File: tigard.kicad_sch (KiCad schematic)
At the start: 91 parts, among them J1 USB_C_Receptacle_USB2.0, J2 JTAG, J3 UART, J4 SPI, J5 CORTEX, J6 LA, J7 I2C, Q1 BSH103, SW1 TARGET, SW2 MODE, U1 AP7365-18, U2 AP7365-33, U3 FT2232HQ, U4 93LC46BT-I/OT, U5 SN74LVC8T245, U6 SN74LVC8T245, Y1 12MHz

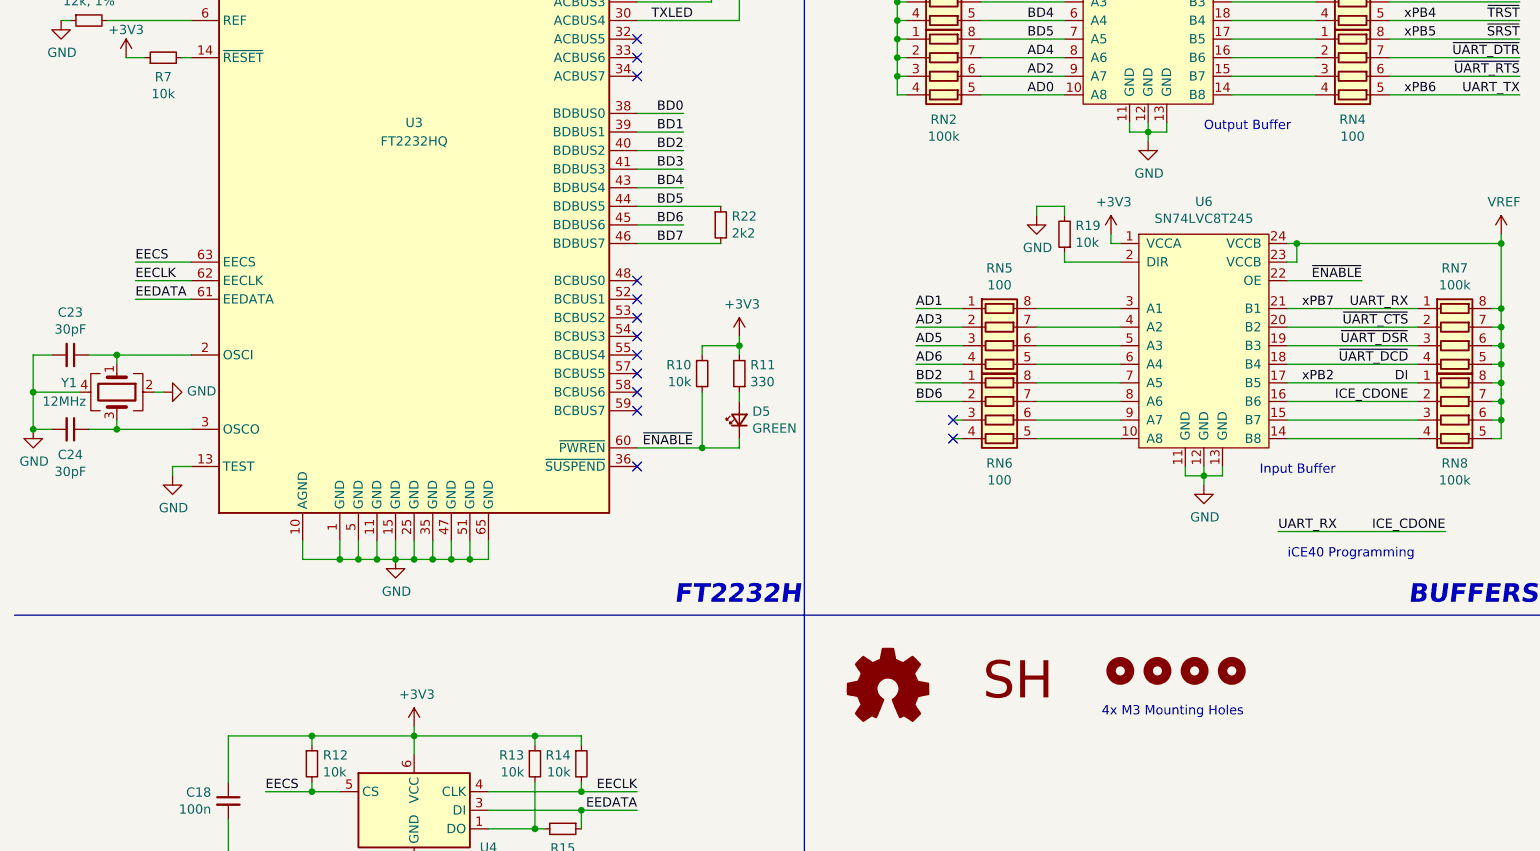
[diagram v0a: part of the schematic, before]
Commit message: tigard-lts: first pass at placement
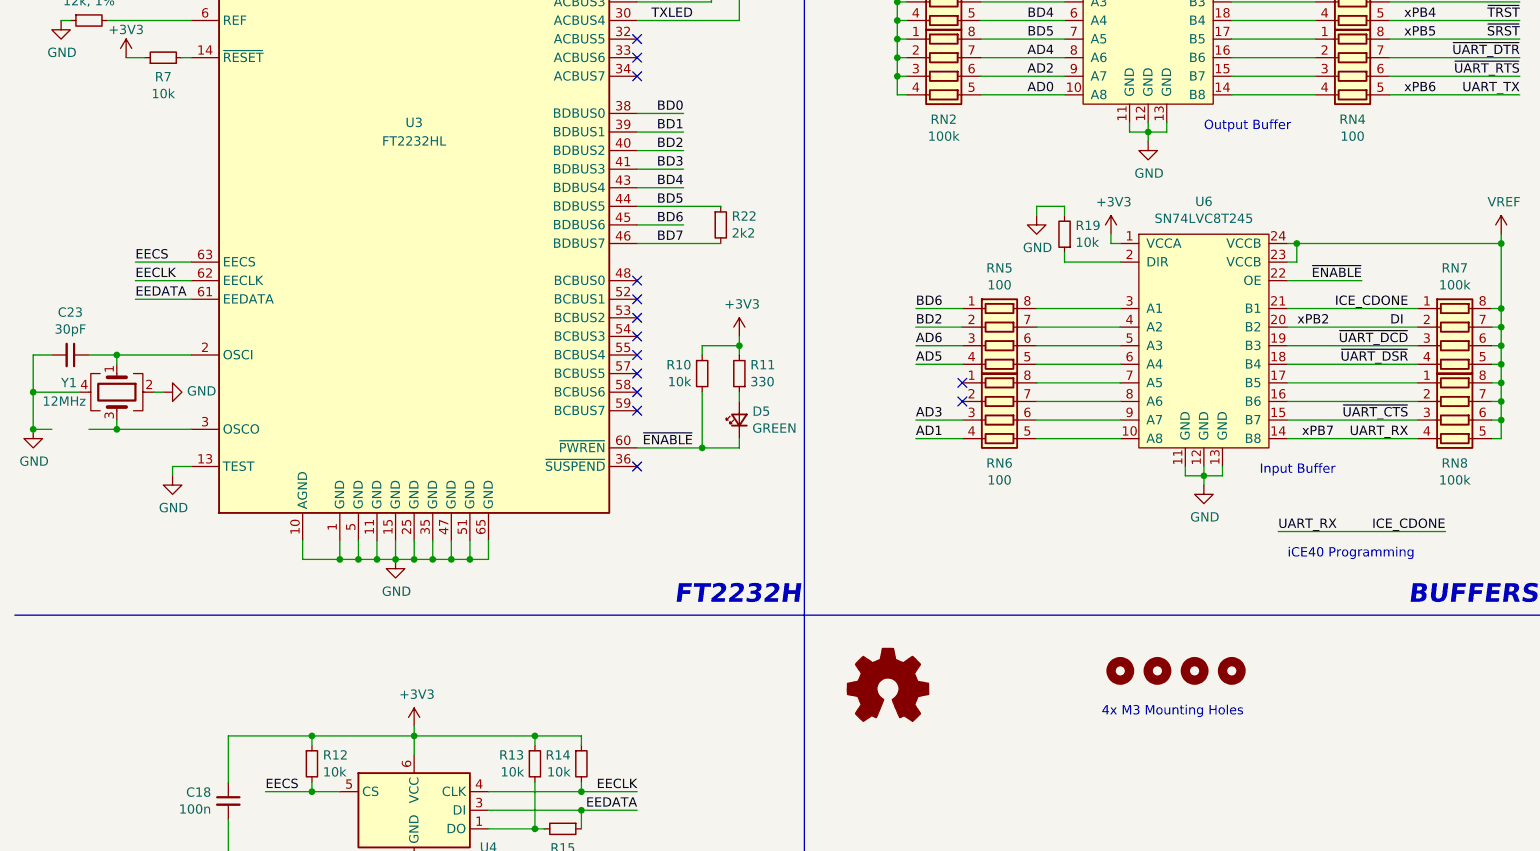
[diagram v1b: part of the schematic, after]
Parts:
- removed C24: 30pF, Capacitor_SMD:C_0402_1005Metric, symbol Device:C_Small
- removed LOGO2: Logo_SH, tigard:Securing_Hardware_Logo, symbol tigard:Logo_SH
- C1, C10, C11, C12, C13, C14, C15, C16, C17, C18, C19, C2, C20, C21, C22, C23, C25, C26, C3, C4, C5, C6, C7, C8, C9: footprint Capacitor_SMD:C_0402_1005Metric -> Capacitor_SMD:C_0805_2012Metric
- D1, D2, D3, D4, D5: footprint LED_SMD:LED_0603_1608Metric -> LED_SMD:LED_0805_2012Metric
- FB1, FB2, FB3: footprint Inductor_SMD:L_0402_1005Metric -> Inductor_SMD:L_0805_2012Metric
- R1, R10, R11, R12, R13, R14, R15, R16, R17, R18, R19, R2, R20, R21, R22, R24, R3, R4, R5, R6, R7, R8, R9: footprint Resistor_SMD:R_0402_1005Metric -> Inductor_SMD:L_0805_2012Metric
- RN1, RN2, RN3, RN4, RN5, RN6, RN7, RN8: footprint tigard:R_Array_Convex_4x0402_RoundRect -> Resistor_SMD:R_Array_Convex_4x0603
- U3: value FT2232HQ -> FT2232HL; footprint Package_DFN_QFN:QFN-64-1EP_9x9mm_P0.5mm_EP4.35x4.35mm_ThermalVias -> Package_QFP:LQFP-64_10x10mm_P0.5mm
- U5, U6: footprint Package_SO:TSSOP-24_4.4x7.8mm_P0.65mm -> Package_SO:SOIC-24W_7.5x15.4mm_P1.27mm
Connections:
- net AD1: now also RN6.4 (R4.1); no longer RN5.1 (R1.1)
- net AD3: now also RN6.3 (R3.1); no longer RN5.2 (R2.1)
- net AD5: now also RN5.4 (R4.1); no longer RN5.3 (R3.1)
- net AD6: now also RN5.3 (R3.1); no longer RN5.4 (R4.1)
- net BD2: now also RN5.2 (R2.1); no longer RN6.1 (R1.1)
- net BD6: now also RN5.1 (R1.1); no longer RN6.2 (R2.1)
- net DI: now also RN7.2 (R2.1), U6.20 (B2); no longer RN8.1 (R1.1), U6.17 (B5)
- net ICE_CDONE: now also RN8.4 (R4.1), U6.14 (B8); no longer RN8.2 (R2.1), U6.16 (B6)
- net ~{UART_CTS}: now also RN8.3 (R3.1), U6.15 (B7); no longer RN7.2 (R2.1), U6.20 (B2)
- net ~{UART_DCD}: now also RN7.3 (R3.1), U6.19 (B3); no longer RN7.4 (R4.1), U6.18 (B4)
- net ~{UART_DSR}: now also RN7.4 (R4.1), U6.18 (B4); no longer RN7.3 (R3.1), U6.19 (B3)
- new net: RN8.2 (R2.1), U6.16 (B6)
- new net: RN8.1 (R1.1), U6.17 (B5)

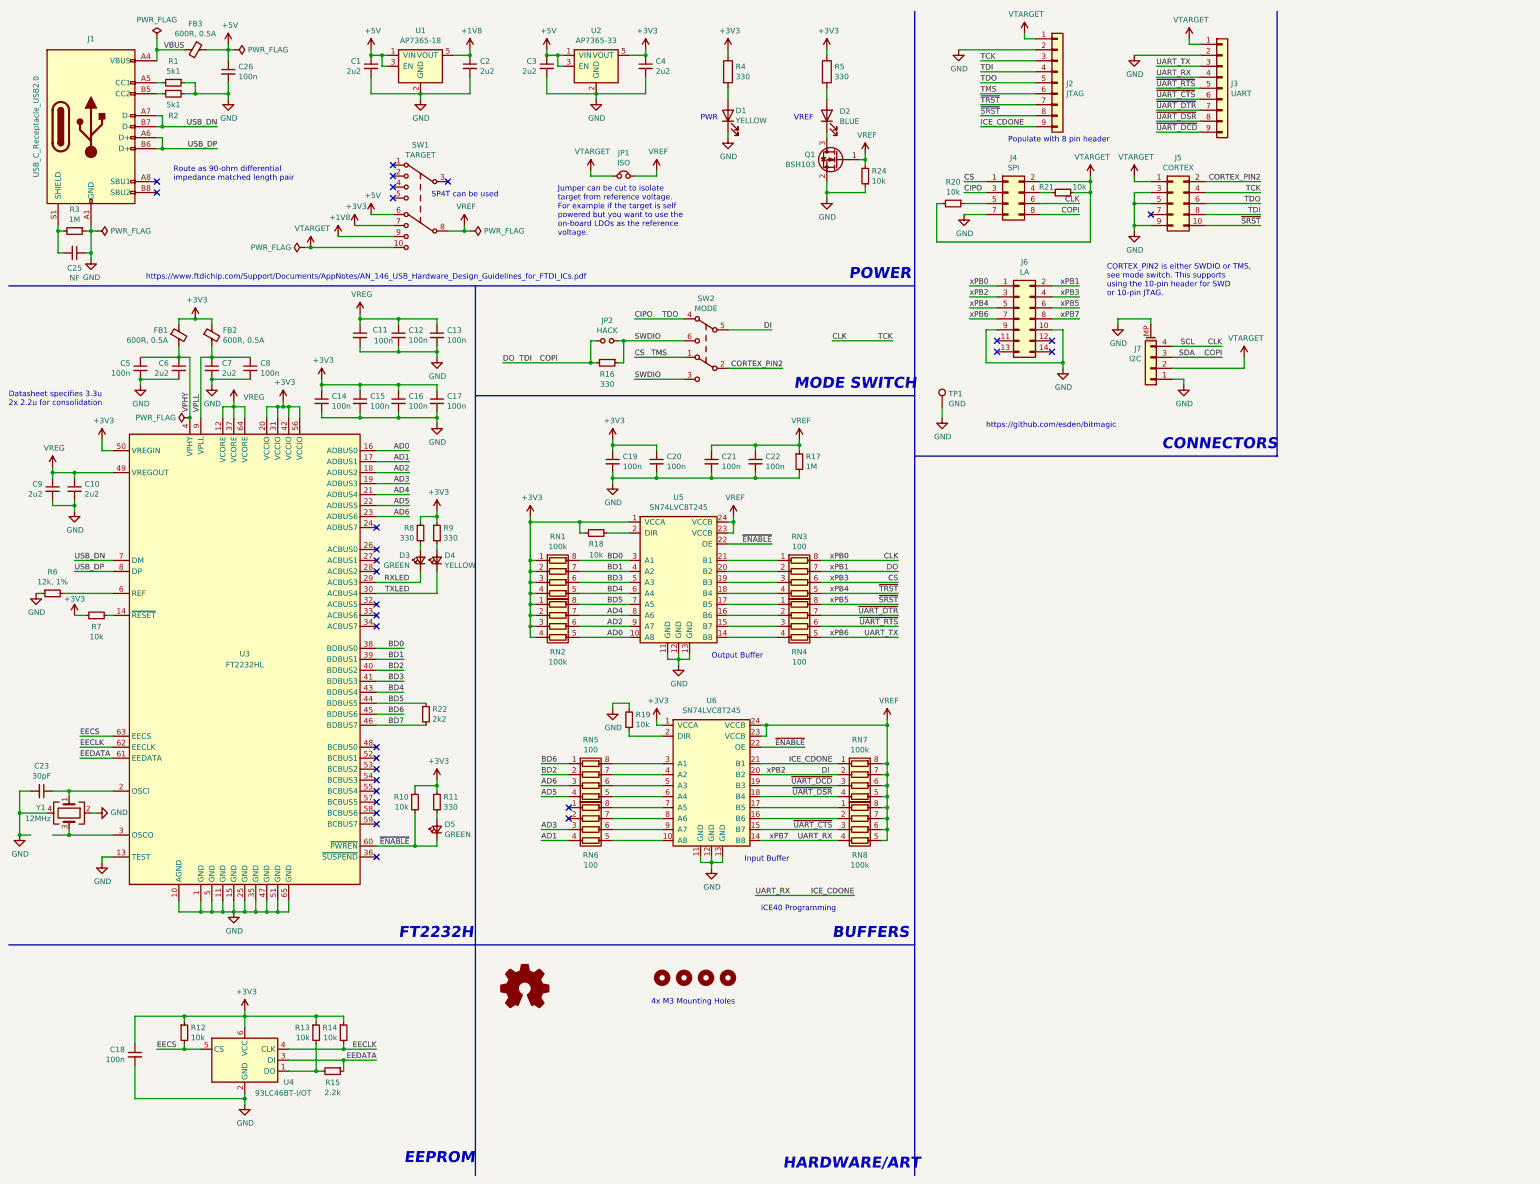
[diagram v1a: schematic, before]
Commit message: tomk-tigard-lts: progress commit - board outline
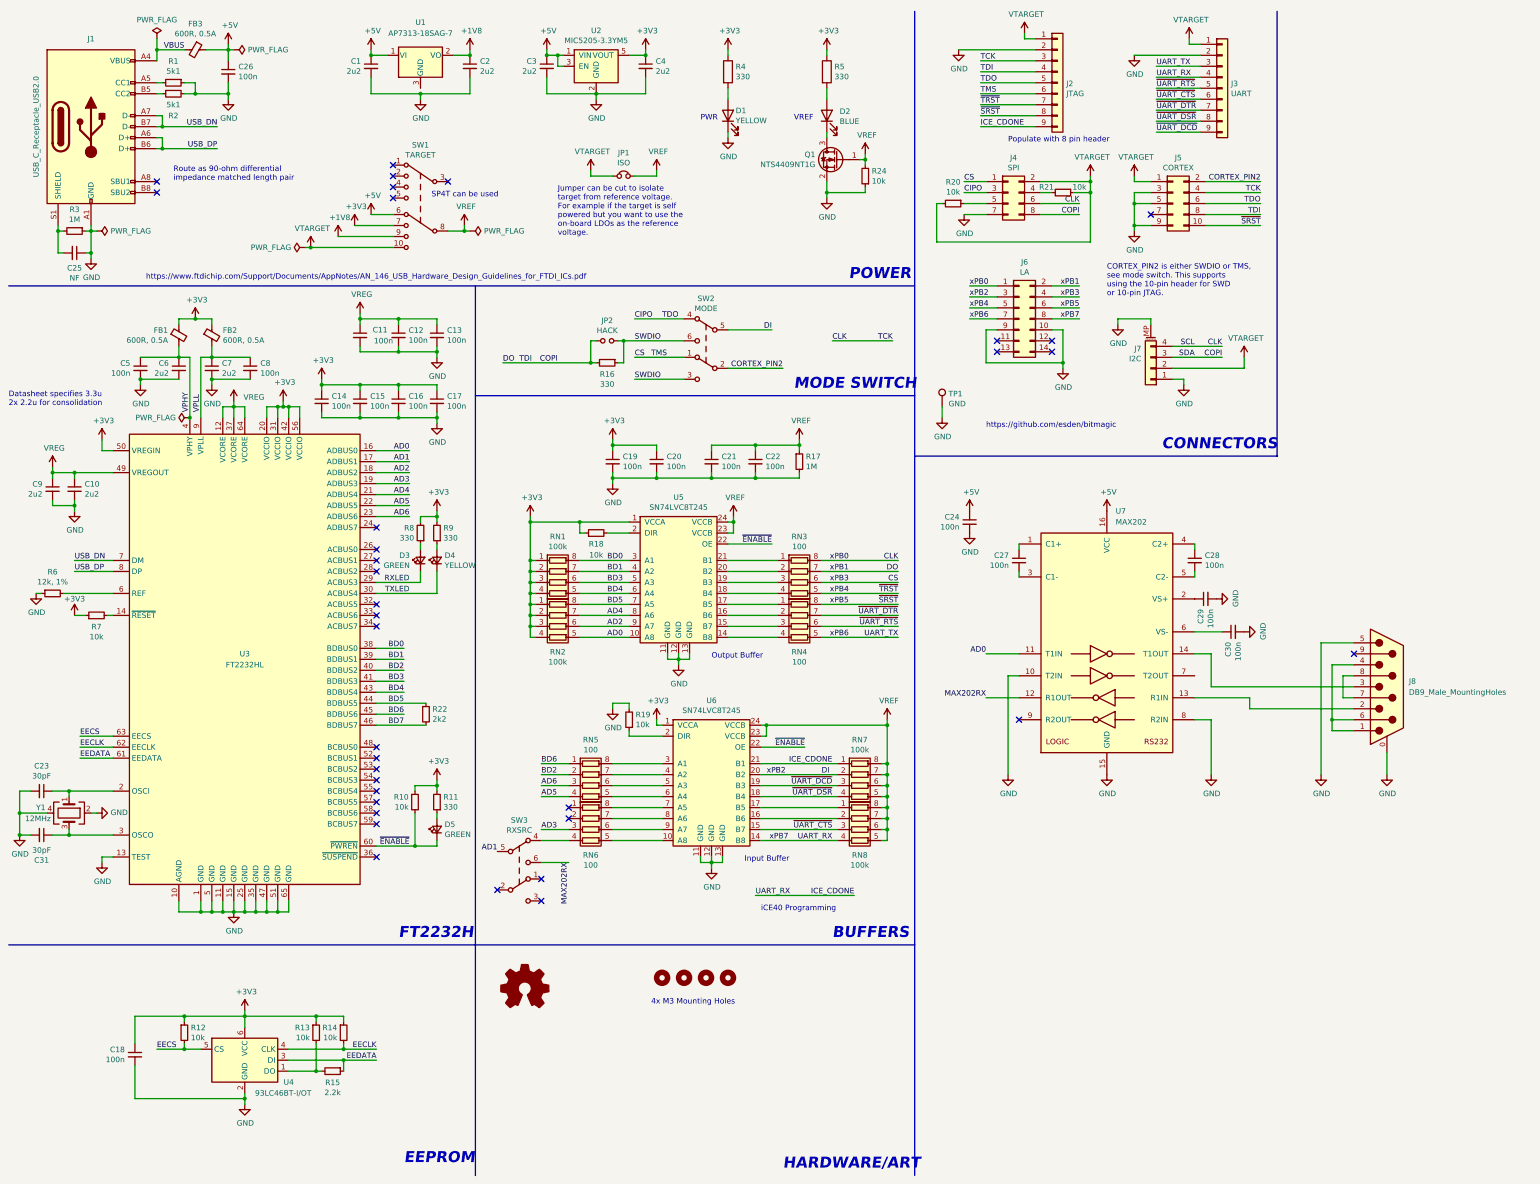
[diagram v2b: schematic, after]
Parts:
- removed U1: AP7365-18, tigard:SOT-23-5_RoundRect, symbol tigard:AP7365-18
- added C24, C27, C28, C29, C30: 100n, Capacitor_SMD:C_0805_2012Metric, symbol Device:C_Small
- added C31: 30pF, Capacitor_SMD:C_0805_2012Metric, symbol Device:C_Small
- added J8: DB9_Male_MountingHoles, Connector_Dsub:DSUB-9_Male_Horizontal_P2.77x2.84mm_EdgePinOffset7.70mm_Housed_MountingHolesOffset9.12mm, symbol Connector:DB9_Male_MountingHoles
- added SW3: RXSRC, tigard:SW_CuK_JS202011CQN_DPDT_Straight, symbol tigard:SW_DPDT
- added U1: AP7313-18SAG-7, tigard:SOT-23_RoundRect, symbol tigard:AP7313-18SAG-7
- added U7: MAX202, Package_SO:SOIC-16_3.9x9.9mm_P1.27mm, symbol Interface_UART:MAX202
- Q1: value BSH103 -> NTS4409NT1G; footprint tigard:SOT-23_RoundRect -> Package_TO_SOT_SMD:SOT-323_SC-70
- U2: value AP7365-33 -> MIC5205-3.3YM5
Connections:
- net +1V8: now also U1.2 (VO)
- net +5V: now also C24.1, U1.1 (VI), U7.16 (VCC)
- net AD0: now also U7.11 (T1IN)
- net AD1: now also SW3.5; no longer RN6.4 (R4.1)
- net GND: now also C24.2, C29.2, C30.2, C31.2, J8.0 (PAD), J8.5, U7.10 (T2IN), U7.15 (GND), U7.8 (R2IN)
- net at U3.3 (OSCO), Y1.3: now also C31.1
- new net: RN6.4 (R4.1), SW3.4
- new net: C28.1, U7.4 (C2+)
- new net: C28.2, U7.5 (C2-)
- new net: C30.1, U7.6 (VS-)
- new net: C27.1, U7.1 (C1+)
- new net: C27.2, U7.3 (C1-)
- new net: J8.1, J8.4, J8.6
- new net: J8.2, U7.13 (R1IN)
- new net: J8.3, U7.14 (T1OUT)
- new net: J8.7, J8.8
- new net: C29.1, U7.2 (VS+)
- new net MAX202RX: SW3.6, U7.12 (R1OUT)
- no-connect marks 30 -> 35

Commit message: tigard-lts: progress commit
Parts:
- added LOGO?: Logo_Open_Hardware_Small, tigard:Tigard_Logo, symbol Graphic:Logo_Open_Hardware_Small
- added R23: 0R, Inductor_SMD:L_0805_2012Metric, symbol Device:R_Small
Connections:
- net AD0: now also RN2.8 (R1.2); no longer RN2.5 (R4.2)
- net AD1: now also R23.2
- net AD2: now also RN2.7 (R2.2); no longer RN2.6 (R3.2)
- net AD4: now also RN2.6 (R3.2); no longer RN2.7 (R2.2)
- net BD0: now also RN2.5 (R4.2), U5.7 (A5); no longer RN1.8 (R1.2), U5.3 (A1)
- net BD1: now also RN1.8 (R1.2), U5.6 (A4); no longer RN1.7 (R2.2), U5.4 (A2)
- net BD3: now also RN1.7 (R2.2); no longer RN1.6 (R3.2)
- net BD4: now also RN1.6 (R3.2), U5.4 (A2); no longer RN1.5 (R4.2), U5.6 (A4)
- net BD5: now also RN1.5 (R4.2), U5.3 (A1); no longer RN2.8 (R1.2), U5.7 (A5)
- net CLK: now also RN4.8 (R1.2); no longer RN3.8 (R1.2)
- net COPI: now also RN3.5 (R4.2); no longer RN3.7 (R2.2)
- net xPB4: now also RN3.7 (R2.2); no longer RN3.5 (R4.2)
- net xPB5: now also RN3.8 (R1.2); no longer RN4.8 (R1.2)
- net at RN6.4 (R4.1), SW3.4: now also R23.1
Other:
- moved on the sheet: RN1, RN2

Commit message: tomk-tigard-lts: progress commit
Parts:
- gave numbers to parts that had none: 1
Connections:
- net at C23.1, Y1.1: now also U3.3 (OSCO); no longer U3.2 (OSCI)
- net at C31.1, Y1.3: now also U3.2 (OSCI); no longer U3.3 (OSCO)
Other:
- moved on the sheet: C23, C31, Y1
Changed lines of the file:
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@@
     (pin "1")
   )
-  (symbol (lib_id "Device:Crystal_GND24") (at 27.94 199.39 270) (unit 1)
+  (symbol (lib_id "Device:Crystal_GND24") (at 27.94 199.39 90) (unit 1)
     (in_bom yes) (on_board yes)
-    (property "Reference" "Y1" (id 0) (at 20.32 198.12 90)
+    (property "Reference" "Y1" (id 0) (at 21.59 198.12 90)
       (effects (font (size 1.27 1.27)) (justify left))
     )
-    (property "Value" "12MHz" (id 1) (at 17.78 200.66 90)
+    (property "Value" "12MHz" (id 1) (at 24.13 200.66 90)
       (effects (font (size 1.27 1.27)) (justify left))
     )
@@
     (pin "1")
   )
-  (symbol (lib_id "Device:C_Small") (at 21.59 194.31 270) (unit 1)
+  (symbol (lib_id "Device:C_Small") (at 21.59 204.47 270) (mirror x) (unit 1)
     (in_bom yes) (on_board yes)
-    (property "Reference" "C23" (id 0) (at 21.59 188.4934 90))
-    (property "Value" "30pF" (id 1) (at 21.59 190.8048 90))
-    (property "Footprint" "Capacitor_SMD:C_0805_2012Metric" (id 2) (at 21.59 194.31 0)
+    (property "Reference" "C23" (id 0) (at 21.59 210.2866 90))
+    (property "Value" "30pF" (id 1) (at 21.59 207.9752 90))
+    (property "Footprint" "Capacitor_SMD:C_0805_2012Metric" (id 2) (at 21.59 204.47 0)
       (effects (font (size 1.27 1.27)) hide)
     )
-    (property "Datasheet" "~" (id 3) (at 21.59 194.31 0)
+    (property "Datasheet" "~" (id 3) (at 21.59 204.47 0)
       (effects (font (size 1.27 1.27)) hide)
     )
-    (property "P/N" "CL05C300JB5NNNC" (id 4) (at 21.59 194.31 90)
+    (property "P/N" "CL05C300JB5NNNC" (id 4) (at 21.59 204.47 90)
       (effects (font (size 1.27 1.27)) hide)
     )
-    (property "LCSC" "C159804" (id 5) (at 21.59 194.31 90)
+    (property "LCSC" "C159804" (id 5) (at 21.59 204.47 90)
       (effects (font (size 1.27 1.27)) hide)
     )
-    (property "Key" "cap-cer-0402-30pF" (id 6) (at 21.59 194.31 90)
+    (property "Key" "cap-cer-0402-30pF" (id 6) (at 21.59 204.47 90)
       (effects (font (size 1.27 1.27)) hide)
     )
@@
     (pin "2")
   )
-  (symbol (lib_id "Device:C_Small") (at 21.59 204.47 270) (mirror x) (unit 1)
+  (symbol (lib_id "Device:C_Small") (at 21.59 194.31 270) (unit 1)
     (in_bom yes) (on_board yes)
-    (property "Reference" "C31" (id 0) (at 21.59 210.2866 90))
-    (property "Value" "30pF" (id 1) (at 21.59 207.9752 90))
-    (property "Footprint" "Capacitor_SMD:C_0805_2012Metric" (id 2) (at 21.59 204.47 0)
+    (property "Reference" "C31" (id 0) (at 21.59 188.4934 90))
+    (property "Value" "30pF" (id 1) (at 21.59 190.8048 90))
+    (property "Footprint" "Capacitor_SMD:C_0805_2012Metric" (id 2) (at 21.59 194.31 0)
       (effects (font (size 1.27 1.27)) hide)
     )
-    (property "Datasheet" "~" (id 3) (at 21.59 204.47 0)
+    (property "Datasheet" "~" (id 3) (at 21.59 194.31 0)
       (effects (font (size 1.27 1.27)) hide)
     )
-    (property "P/N" "CL05C300JB5NNNC" (id 4) (at 21.59 204.47 90)
+    (property "P/N" "CL05C300JB5NNNC" (id 4) (at 21.59 194.31 90)
       (effects (font (size 1.27 1.27)) hide)
     )
-    (property "LCSC" "C159804" (id 5) (at 21.59 204.47 90)
+    (property "LCSC" "C159804" (id 5) (at 21.59 194.31 90)
       (effects (font (size 1.27 1.27)) hide)
     )
-    (property "Key" "cap-cer-0402-30pF" (id 6) (at 21.59 204.47 90)
+    (property "Key" "cap-cer-0402-30pF" (id 6) (at 21.59 194.31 90)
       (effects (font (size 1.27 1.27)) hide)
     )
@@
   (symbol (lib_id "Graphic:Logo_Open_Hardware_Small") (at 133.35 255.905 0) (unit 1)
     (in_bom yes) (on_board yes)
-    (property "Reference" "LOGO?" (id 0) (at 133.35 248.92 0)
+    (property "Reference" "LOGO2" (id 0) (at 133.35 248.92 0)
       (effects (font (size 1.27 1.27)) hide)
     )
@@
     )
     (path "/9c8a3ca5-ebe7-4bab-b1b4-1877feaec474"
-      (reference "LOGO?") (unit 1) (value "Logo_Open_Hardware_Small") (footprint "tigard:Tigard_Logo")
+      (reference "LOGO2") (unit 1) (value "Logo_Open_Hardware_Small") (footprint "tigard:Tigard_Logo")
     )
     (path "/00000000-0000-0000-0000-00005ec0037d"
